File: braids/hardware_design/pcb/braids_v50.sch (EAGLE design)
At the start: 120 parts, among them IC1 74HC595D, IC10 TL072, IC2 74HC595D, IC3 LM4040B25, IC4 MCP3204, IC5 DAC8551, IC6 LM1117-3.3, IC7 MCP6004, IC8 LM4040B10, IC9 TL074D, J1 PJ301_THONKICONN6, J2 PJ301_THONKICONN6, J3 PJ301_THONKICONN6, J4 PJ301_THONKICONN6, J5 PJ301_THONKICONN6, J6 PJ301_THONKICONN6, Q1 MMBT3904, Q2 MMBT3904, Q3 MMBT3904, Q4 MMBT3904, Q5 8MHz, Q6 MMBT3904, SW1 EC12E_SW, SW2 EVQQ2, SW3 EVQQ2

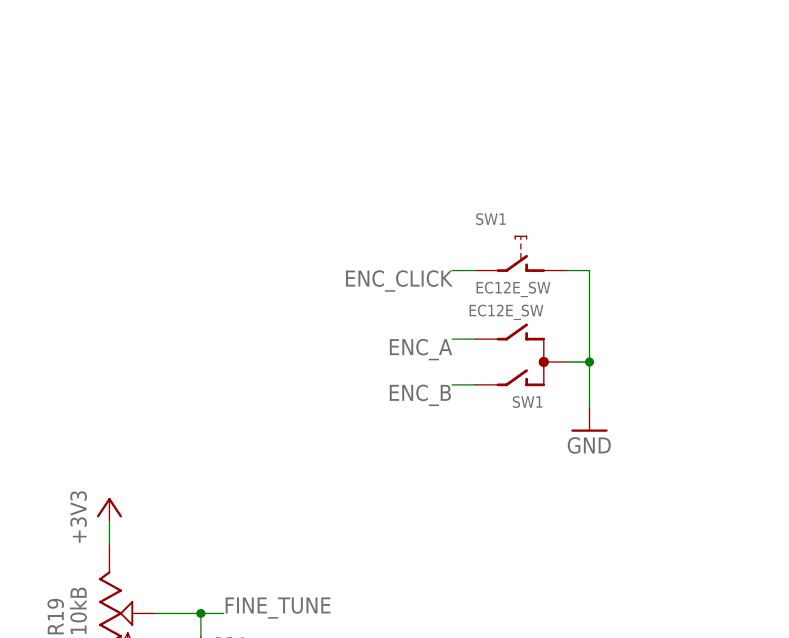
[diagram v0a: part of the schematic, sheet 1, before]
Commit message: make the encoder A/B orientation a build time setting with solder jumpers
Signed-off-by: vladimir <vladimir@pantelic.net>
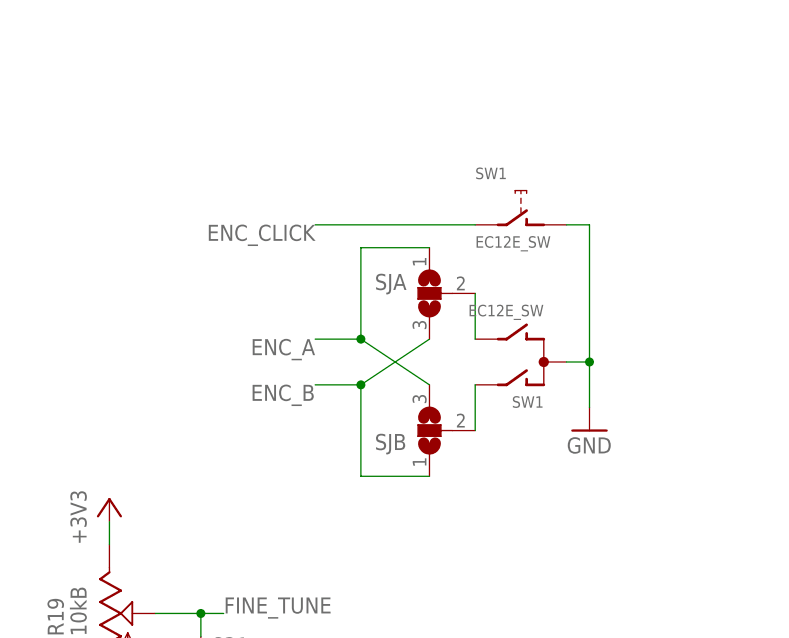
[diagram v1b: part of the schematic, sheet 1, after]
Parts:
- added SJA, SJB: (no value), jumper:SJ2W
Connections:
- new net N$11: SJB.2, SW1G$1.A
- new net N$76: SJA.2, SW1G$1.B
- net ENC_A: now also SJA.1, SJB.3; no longer SW1G$1.B
- net ENC_B: now also SJA.3, SJB.1; no longer SW1G$1.A
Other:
- moved on the sheet: SW1
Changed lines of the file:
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@@
 <part name="SUPPLY3" library="supply2" deviceset="VEE" device=""/>
 <part name="FRAME2" library="frames" deviceset="A3L-LOC" device=""/>
+<part name="SJB" library="jumper" deviceset="SJ2W" device=""/>
+<part name="SJA" library="jumper" deviceset="SJ2W" device=""/>
 </parts>
 <sheets>
@@
 <instance part="GND6" gate="1" x="157.48" y="-38.1"/>
 <instance part="SW1" gate="G$1" x="-124.46" y="10.16" rot="R90"/>
-<instance part="SW1" gate="G$2" x="-127" y="20.32"/>
+<instance part="SW1" gate="G$2" x="-127" y="25.4"/>
 <instance part="R3" gate="G$1" x="55.88" y="-27.94"/>
 <instance part="R11" gate="G$1" x="83.82" y="-27.94"/>
@@
 <instance part="C31" gate="G$1" x="-162.56" y="-22.86"/>
 <instance part="GND30" gate="1" x="-162.56" y="-33.02"/>
+<instance part="SJB" gate="G$1" x="-137.16" y="2.54" rot="R180"/>
+<instance part="SJA" gate="G$1" x="-137.16" y="17.78" rot="MR0"/>
 </instances>
 <busses>
@@
 <wire x1="-121.92" y1="10.16" x2="-119.38" y2="10.16" width="0.1524" layer="91"/>
 <wire x1="-119.38" y1="10.16" x2="-119.38" y2="5.08" width="0.1524" layer="91"/>
-<wire x1="-119.38" y1="20.32" x2="-119.38" y2="10.16" width="0.1524" layer="91"/>
-<wire x1="-121.92" y1="20.32" x2="-119.38" y2="20.32" width="0.1524" layer="91"/>
+<wire x1="-119.38" y1="25.4" x2="-119.38" y2="10.16" width="0.1524" layer="91"/>
+<wire x1="-121.92" y1="25.4" x2="-119.38" y2="25.4" width="0.1524" layer="91"/>
 <junction x="-119.38" y="10.16"/>
 <pinref part="SW1" gate="G$1" pin="C"/>
@@
 </segment>
 <segment>
-<wire x1="-132.08" y1="20.32" x2="-134.62" y2="20.32" width="0.1524" layer="91"/>
-<label x="-134.62" y="20.32" size="1.778" layer="95" rot="R180"/>
+<wire x1="-132.08" y1="25.4" x2="-149.86" y2="25.4" width="0.1524" layer="91"/>
+<label x="-149.86" y="25.4" size="1.778" layer="95" rot="R180"/>
 <pinref part="SW1" gate="G$2" pin="2"/>
 </segment>
@@
 </segment>
 <segment>
-<wire x1="-132.08" y1="12.7" x2="-134.62" y2="12.7" width="0.1524" layer="91"/>
-<label x="-134.62" y="12.7" size="1.778" layer="95" rot="R180"/>
-<pinref part="SW1" gate="G$1" pin="B"/>
+<label x="-149.86" y="12.7" size="1.778" layer="95" rot="R180"/>
+<pinref part="SJA" gate="G$1" pin="1"/>
+<wire x1="-137.16" y1="22.86" x2="-144.78" y2="22.86" width="0.1524" layer="91"/>
+<wire x1="-144.78" y1="22.86" x2="-144.78" y2="12.7" width="0.1524" layer="91"/>
+<pinref part="SJB" gate="G$1" pin="3"/>
+<wire x1="-137.16" y1="7.62" x2="-144.78" y2="12.7" width="0.1524" layer="91"/>
+<wire x1="-144.78" y1="12.7" x2="-149.86" y2="12.7" width="0.1524" layer="91"/>
+<junction x="-144.78" y="12.7"/>
 </segment>
 </net>
@@
 </segment>
 <segment>
-<wire x1="-132.08" y1="7.62" x2="-134.62" y2="7.62" width="0.1524" layer="91"/>
-<label x="-134.62" y="7.62" size="1.778" layer="95" rot="R180"/>
-<pinref part="SW1" gate="G$1" pin="A"/>
+<label x="-149.86" y="7.62" size="1.778" layer="95" rot="R180"/>
+<pinref part="SJB" gate="G$1" pin="1"/>
+<wire x1="-137.16" y1="-2.54" x2="-144.78" y2="-2.54" width="0.1524" layer="91"/>
+<wire x1="-144.78" y1="-2.54" x2="-144.78" y2="7.62" width="0.1524" layer="91"/>
+<pinref part="SJA" gate="G$1" pin="3"/>
+<wire x1="-144.78" y1="7.62" x2="-137.16" y2="12.7" width="0.1524" layer="91"/>
+<wire x1="-144.78" y1="7.62" x2="-149.86" y2="7.62" width="0.1524" layer="91"/>
+<junction x="-144.78" y="7.62"/>
 </segment>
 </net>
@@
 </segment>
 </net>
+<net name="N$76" class="0">
+<segment>
+<pinref part="SW1" gate="G$1" pin="B"/>
+<pinref part="SJA" gate="G$1" pin="2"/>
+<wire x1="-132.08" y1="17.78" x2="-132.08" y2="12.7" width="0.1524" layer="91"/>
+</segment>
+</net>
+<net name="N$11" class="0">
+<segment>
+<pinref part="SW1" gate="G$1" pin="A"/>
+<pinref part="SJB" gate="G$1" pin="2"/>
+<wire x1="-132.08" y1="2.54" x2="-132.08" y2="7.62" width="0.1524" layer="91"/>
+</segment>
+</net>

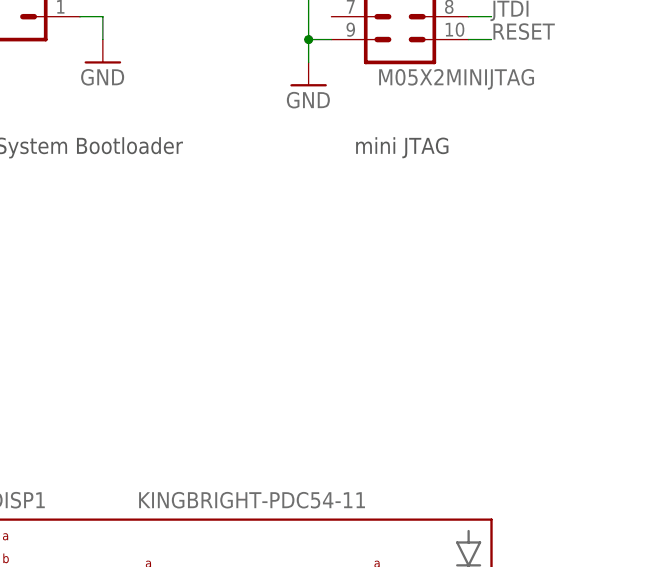
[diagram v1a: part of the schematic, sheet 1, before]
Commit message: add a 6-pin combined SWD/UART header
Signed-off-by: Vladimir Pantelic <vladimir@pantelic.net>
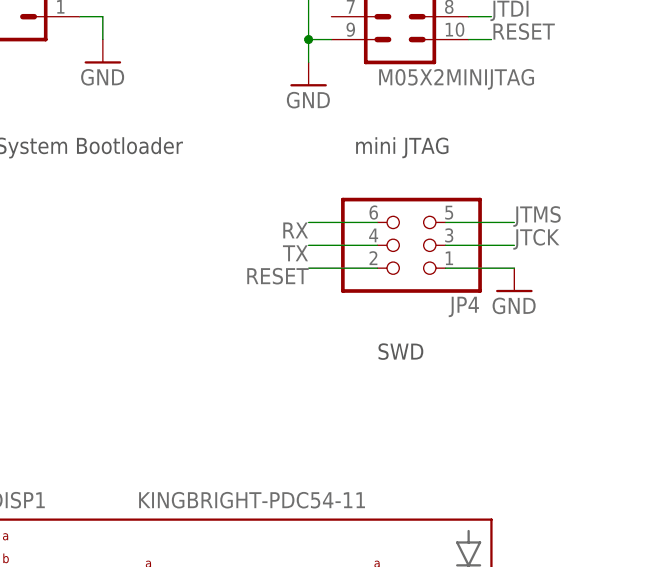
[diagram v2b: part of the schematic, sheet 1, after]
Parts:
- added JP4: (no value), vpme_eurorack:PINHD-2X3"
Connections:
- net GND: now also JP4.1
- net JTCK: now also JP4.3
- net JTMS: now also JP4.5
- net RESET: now also JP4.2
- net RX: now also JP4.6
- net TX: now also JP4.4
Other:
- note added: "SWD"
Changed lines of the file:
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@@
 <part name="SJB" library="jumper" deviceset="SJ2W" device=""/>
 <part name="SJA" library="jumper" deviceset="SJ2W" device=""/>
+<part name="JP4" library="vpme_eurorack" deviceset="PINHD-2X3" device="&quot;"/>
+<part name="GND44" library="SparkFun" deviceset="GND" device=""/>
 </parts>
 <sheets>
@@
 <text x="142.24" y="-76.2" size="2.54" layer="94">Digital section</text>
 <text x="-30.48" y="132.08" size="1.27" layer="97">grounded on v4.0 or above</text>
+<text x="147.32" y="43.18" size="1.778" layer="97">SWD</text>
 </plain>
 <instances>
@@
 <instance part="SJB" gate="G$1" x="-137.16" y="2.54" rot="R180"/>
 <instance part="SJA" gate="G$1" x="-137.16" y="17.78" rot="MR0"/>
+<instance part="JP4" gate="A" x="152.4" y="55.88" rot="R180"/>
+<instance part="GND44" gate="1" x="162.56" y="50.8"/>
 </instances>
 <busses>
@@
 <pinref part="GND30" gate="1" pin="GND"/>
 </segment>
+<segment>
+<pinref part="JP4" gate="A" pin="1"/>
+<wire x1="162.56" y1="53.34" x2="154.94" y2="53.34" width="0.1524" layer="91"/>
+<pinref part="GND44" gate="1" pin="GND"/>
+</segment>
 </net>
 <net name="+3V3" class="0">
@@
 <pinref part="JP2" gate="G$1" pin="10"/>
 </segment>
+<segment>
+<pinref part="JP4" gate="A" pin="2"/>
+<wire x1="147.32" y1="53.34" x2="139.7" y2="53.34" width="0.1524" layer="91"/>
+<label x="139.7" y="53.34" size="1.778" layer="95" rot="R180"/>
+</segment>
 </net>
 <net name="RX" class="0">
@@
 <pinref part="JP3" gate="G$1" pin="4"/>
 </segment>
+<segment>
+<pinref part="JP4" gate="A" pin="6"/>
+<wire x1="147.32" y1="58.42" x2="139.7" y2="58.42" width="0.1524" layer="91"/>
+<label x="139.7" y="58.42" size="1.778" layer="95" rot="R180"/>
+</segment>
 </net>
 <net name="TX" class="0">
@@
 <pinref part="JP3" gate="G$1" pin="5"/>
 </segment>
+<segment>
+<pinref part="JP4" gate="A" pin="4"/>
+<wire x1="147.32" y1="55.88" x2="139.7" y2="55.88" width="0.1524" layer="91"/>
+<label x="139.7" y="55.88" size="1.778" layer="95" rot="R180"/>
+</segment>
 </net>
 <net name="JTDI" class="0">
@@
 <pinref part="UC1" gate="G$1" pin="PA14/JTCK/SWCLK"/>
 </segment>
+<segment>
+<pinref part="JP4" gate="A" pin="3"/>
+<wire x1="154.94" y1="55.88" x2="162.56" y2="55.88" width="0.1524" layer="91"/>
+<label x="162.56" y="55.88" size="1.778" layer="95"/>
+</segment>
 </net>
 <net name="JTMS" class="0">
@@
 <pinref part="UC1" gate="G$1" pin="PA13/JTMS/SWDIO"/>
 </segment>
-</net>
+<segment>
+<pinref part="JP4" gate="A" pin="5"/>
+<wire x1="154.94" y1="58.42" x2="162.56" y2="58.42" width="0.1524" layer="91"/>
+<label x="162.56" y="58.42" size="1.778" layer="95"/>
+</segment>
+</net>
